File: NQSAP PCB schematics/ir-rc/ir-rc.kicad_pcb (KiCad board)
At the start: 2 copper layers, 102 x 96 mm, 6 parts, among them J1 Bus, J2 Bus, J3 Conn_02x08, J4 Conn_02x08, J5 Conn_02x08, J6 Conn_02x08

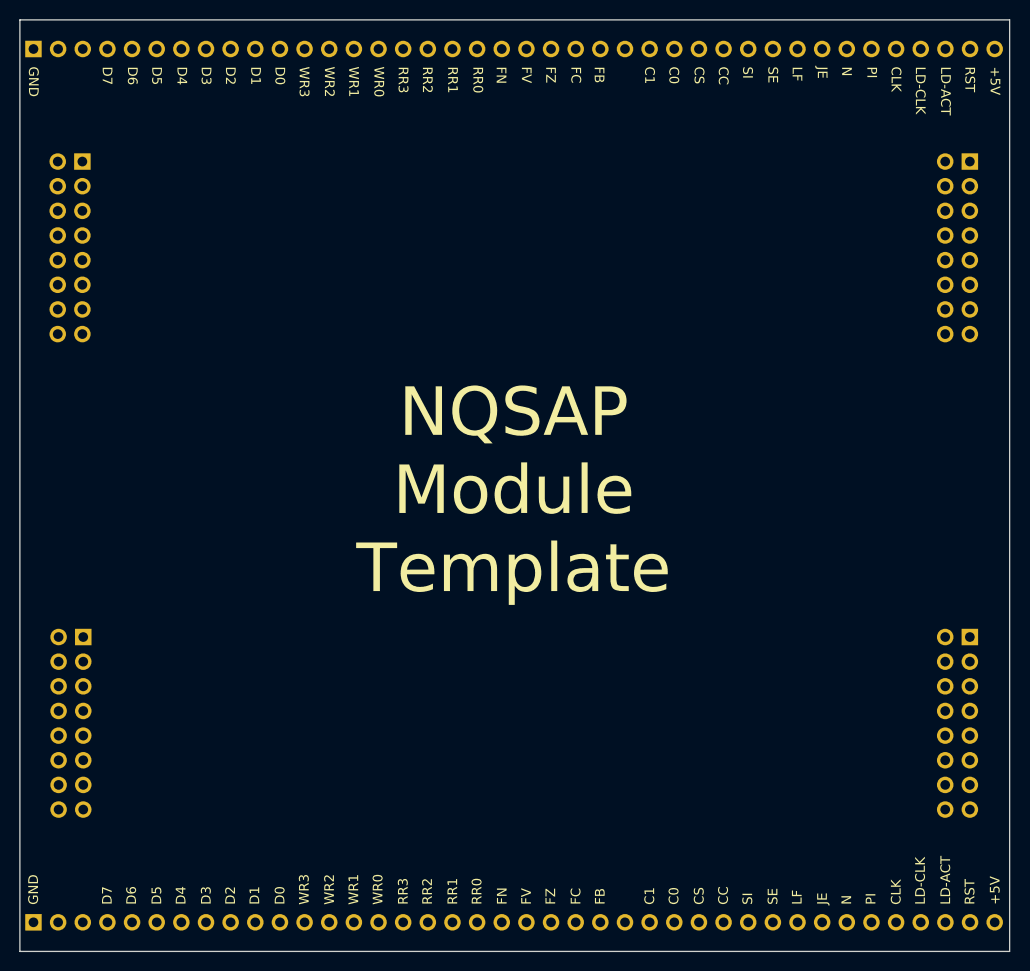
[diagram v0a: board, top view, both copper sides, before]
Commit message: Add Microcode and IR/RC modules.  Add clock circuit to Loader module.
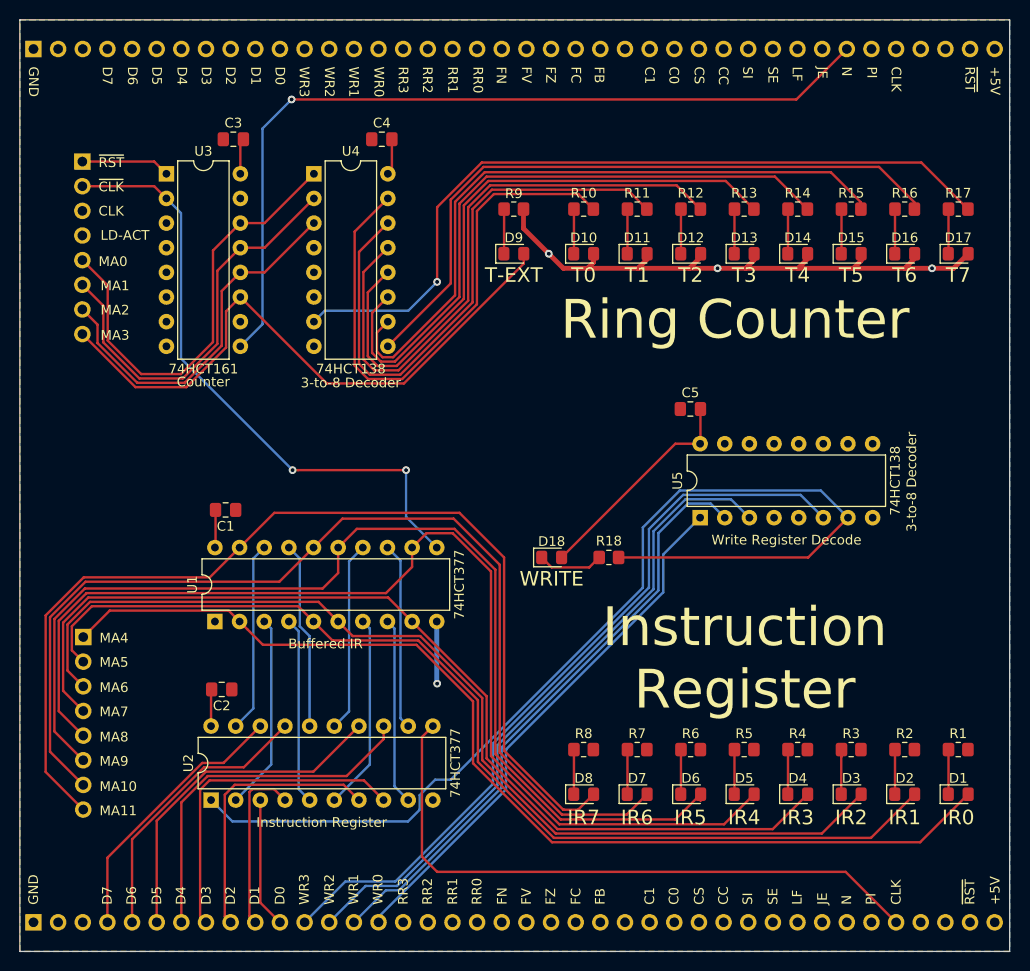
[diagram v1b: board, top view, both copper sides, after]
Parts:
- removed J5, J6: Conn_02x08, Connector_PinHeader_2.54mm:PinHeader_2x08_P2.54mm_Vertical
- added C1: 0.1uF, Capacitor_SMD:C_0805_2012Metric_Pad1.18x1.45mm_HandSolder, F.Cu at (106.2, 93.5)
- added C2: 0.1uF, Capacitor_SMD:C_0805_2012Metric_Pad1.18x1.45mm_HandSolder, F.Cu at (105.8, 112.0)
- added C3: 0.1uF, Capacitor_SMD:C_0805_2012Metric_Pad1.18x1.45mm_HandSolder, F.Cu at (107.0, 55.3)
- added C4: 0.1uF, Capacitor_SMD:C_0805_2012Metric_Pad1.18x1.45mm_HandSolder, F.Cu at (122.3, 55.3)
- added C5: 0.1uF, Capacitor_SMD:C_0805_2012Metric_Pad1.18x1.45mm_HandSolder, F.Cu at (154.1, 83.1)
- added D1: IR0, LED_SMD:LED_0805_2012Metric_Pad1.15x1.40mm_HandSolder, F.Cu at (181.7, 122.8)
- added D10: T0, LED_SMD:LED_0805_2012Metric_Pad1.15x1.40mm_HandSolder, F.Cu at (143.1, 67.1)
- added D11: T1, LED_SMD:LED_0805_2012Metric_Pad1.15x1.40mm_HandSolder, F.Cu at (148.6, 67.1)
- added D12: T2, LED_SMD:LED_0805_2012Metric_Pad1.15x1.40mm_HandSolder, F.Cu at (154.1, 67.1)
- added D13: T3, LED_SMD:LED_0805_2012Metric_Pad1.15x1.40mm_HandSolder, F.Cu at (159.6, 67.1)
- added D14: T4, LED_SMD:LED_0805_2012Metric_Pad1.15x1.40mm_HandSolder, F.Cu at (165.2, 67.1)
- added D15: T5, LED_SMD:LED_0805_2012Metric_Pad1.15x1.40mm_HandSolder, F.Cu at (170.7, 67.1)
- added D16: T6, LED_SMD:LED_0805_2012Metric_Pad1.15x1.40mm_HandSolder, F.Cu at (176.2, 67.1)
- added D17: T7, LED_SMD:LED_0805_2012Metric_Pad1.15x1.40mm_HandSolder, F.Cu at (181.7, 67.1)
- added D18: WRITE, LED_SMD:LED_0805_2012Metric_Pad1.15x1.40mm_HandSolder, F.Cu at (139.8, 98.4)
- added D2: IR1, LED_SMD:LED_0805_2012Metric_Pad1.15x1.40mm_HandSolder, F.Cu at (176.2, 122.8)
- added D3: IR2, LED_SMD:LED_0805_2012Metric_Pad1.15x1.40mm_HandSolder, F.Cu at (170.7, 122.8)
- added D4: IR3, LED_SMD:LED_0805_2012Metric_Pad1.15x1.40mm_HandSolder, F.Cu at (165.2, 122.8)
- added D5: IR4, LED_SMD:LED_0805_2012Metric_Pad1.15x1.40mm_HandSolder, F.Cu at (159.6, 122.8)
- added D6: IR5, LED_SMD:LED_0805_2012Metric_Pad1.15x1.40mm_HandSolder, F.Cu at (154.1, 122.8)
- added D7: IR6, LED_SMD:LED_0805_2012Metric_Pad1.15x1.40mm_HandSolder, F.Cu at (148.6, 122.8)
- added D8: IR7, LED_SMD:LED_0805_2012Metric_Pad1.15x1.40mm_HandSolder, F.Cu at (143.1, 122.8)
- added D9: T-EXT, LED_SMD:LED_0805_2012Metric_Pad1.15x1.40mm_HandSolder, F.Cu at (135.9, 67.1)
- added R1: R-GRN, Resistor_SMD:R_0805_2012Metric_Pad1.20x1.40mm_HandSolder, F.Cu at (181.7, 118.2)
- added R10: R-YEL, Resistor_SMD:R_0805_2012Metric_Pad1.20x1.40mm_HandSolder, F.Cu at (143.1, 62.5)
- added R11: R-YEL, Resistor_SMD:R_0805_2012Metric_Pad1.20x1.40mm_HandSolder, F.Cu at (148.6, 62.5)
- added R12: R-YEL, Resistor_SMD:R_0805_2012Metric_Pad1.20x1.40mm_HandSolder, F.Cu at (154.1, 62.5)
- added R13: R-YEL, Resistor_SMD:R_0805_2012Metric_Pad1.20x1.40mm_HandSolder, F.Cu at (159.6, 62.5)
- added R14: R-YEL, Resistor_SMD:R_0805_2012Metric_Pad1.20x1.40mm_HandSolder, F.Cu at (165.2, 62.5)
- added R15: R-YEL, Resistor_SMD:R_0805_2012Metric_Pad1.20x1.40mm_HandSolder, F.Cu at (170.7, 62.5)
- added R16: R-YEL, Resistor_SMD:R_0805_2012Metric_Pad1.20x1.40mm_HandSolder, F.Cu at (176.2, 62.5)
- added R17: R-YEL, Resistor_SMD:R_0805_2012Metric_Pad1.20x1.40mm_HandSolder, F.Cu at (181.7, 62.5)
- added R18: R-RED, Resistor_SMD:R_0805_2012Metric_Pad1.20x1.40mm_HandSolder, F.Cu at (145.7, 98.4)
- added R2: R-GRN, Resistor_SMD:R_0805_2012Metric_Pad1.20x1.40mm_HandSolder, F.Cu at (176.2, 118.2)
- added R3: R-GRN, Resistor_SMD:R_0805_2012Metric_Pad1.20x1.40mm_HandSolder, F.Cu at (170.7, 118.2)
- added R4: R-GRN, Resistor_SMD:R_0805_2012Metric_Pad1.20x1.40mm_HandSolder, F.Cu at (165.2, 118.2)
- added R5: R-GRN, Resistor_SMD:R_0805_2012Metric_Pad1.20x1.40mm_HandSolder, F.Cu at (159.6, 118.2)
- added R6: R-GRN, Resistor_SMD:R_0805_2012Metric_Pad1.20x1.40mm_HandSolder, F.Cu at (154.1, 118.2)
- added R7: R-GRN, Resistor_SMD:R_0805_2012Metric_Pad1.20x1.40mm_HandSolder, F.Cu at (148.6, 118.2)
- added R8: R-GRN, Resistor_SMD:R_0805_2012Metric_Pad1.20x1.40mm_HandSolder, F.Cu at (143.1, 118.2)
- added R9: R-WHT, Resistor_SMD:R_0805_2012Metric_Pad1.20x1.40mm_HandSolder, F.Cu at (135.9, 62.5)
- added U1: 74HCT377, Package_DIP:DIP-20_W7.62mm, F.Cu at (105.1, 105.0)
- added U2: 74HCT377, Package_DIP:DIP-20_W7.62mm, F.Cu at (104.7, 123.4)
- added U3: 74HCT161, Package_DIP:DIP-16_W7.62mm, F.Cu at (100.1, 58.9)
- added U4: 74HCT138, Package_DIP:DIP-16_W7.62mm, F.Cu at (115.3, 58.9)
- added U5: 74HCT138, Package_DIP:DIP-16_W7.62mm, F.Cu at (155.1, 94.3)
- J3, J4: footprint Connector_PinHeader_2.54mm:PinHeader_2x08_P2.54mm_Vertical -> Connector_PinHeader_2.54mm:PinHeader_1x08_P2.54mm_Vertical
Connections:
- net +5V renamed VCC
- J1 pad 10: D1 -> Net-(J1-Pad10)
- J1 pad 11: D0 -> Net-(J1-Pad11)
- J1 pad 12: WR3 -> Net-(J1-Pad12)
- J1 pad 13: WR2 -> Net-(J1-Pad13)
- J1 pad 14: WR1 -> Net-(J1-Pad14)
- J1 pad 15: WR0 -> Net-(J1-Pad15)
- J1 pad 16: RR3 -> Net-(J1-Pad16)
- J1 pad 17: RR2 -> Net-(J1-Pad17)
- J1 pad 18: RR1 -> Net-(J1-Pad18)
- J1 pad 19: RR0 -> Net-(J1-Pad19)
- J1 pad 2: NC-2 -> Net-(J1-Pad2)
- J1 pad 20: FN -> Net-(J1-Pad20)
- J1 pad 21: FV -> Net-(J1-Pad21)
- J1 pad 22: FZ -> Net-(J1-Pad22)
- J1 pad 23: FC -> Net-(J1-Pad23)
- J1 pad 24: FB -> Net-(J1-Pad24)
- J1 pad 25: XX0 -> Net-(J1-Pad25)
- J1 pad 26: C1 -> Net-(J1-Pad26)
- J1 pad 27: C0 -> Net-(J1-Pad27)
- J1 pad 28: CS -> Net-(J1-Pad28)
- J1 pad 29: CC -> Net-(J1-Pad29)
- J1 pad 3: NC-1 -> Net-(J1-Pad3)
- J1 pad 30: SI -> Net-(J1-Pad30)
- J1 pad 31: SE -> Net-(J1-Pad31)
- J1 pad 32: LF -> Net-(J1-Pad32)
- J1 pad 33: JE -> Net-(J1-Pad33)
- J1 pad 35: PI -> Net-(J1-Pad35)
- J1 pad 36: CLK -> Net-(J1-Pad36)
- J1 pad 37: LDR-CLK -> Net-(J1-Pad37)
- J1 pad 38: LDR-ACT -> Net-(J1-Pad38)
- J1 pad 39: RST -> Net-(J1-Pad39)
- J1 pad 4: D7 -> Net-(J1-Pad4)
- J1 pad 5: D6 -> Net-(J1-Pad5)
- J1 pad 6: D5 -> Net-(J1-Pad6)
- J1 pad 7: D4 -> Net-(J1-Pad7)
- J1 pad 8: D3 -> Net-(J1-Pad8)
- J1 pad 9: D2 -> Net-(J1-Pad9)
- J2 pad 16: RR3 -> Net-(J2-Pad16)
- J2 pad 17: RR2 -> Net-(J2-Pad17)
- J2 pad 18: RR1 -> Net-(J2-Pad18)
- J2 pad 19: RR0 -> Net-(J2-Pad19)
- J2 pad 2: NC-2 -> Net-(J2-Pad2)
- J2 pad 20: FN -> Net-(J2-Pad20)
- J2 pad 21: FV -> Net-(J2-Pad21)
- J2 pad 22: FZ -> Net-(J2-Pad22)
- J2 pad 23: FC -> Net-(J2-Pad23)
- J2 pad 24: FB -> Net-(J2-Pad24)
- J2 pad 25: XX0 -> Net-(J2-Pad25)
- J2 pad 26: C1 -> Net-(J2-Pad26)
- J2 pad 27: C0 -> Net-(J2-Pad27)
- J2 pad 28: CS -> Net-(J2-Pad28)
- J2 pad 29: CC -> Net-(J2-Pad29)
- J2 pad 3: NC-1 -> Net-(J2-Pad3)
- J2 pad 30: SI -> Net-(J2-Pad30)
- J2 pad 31: SE -> Net-(J2-Pad31)
- J2 pad 32: LF -> Net-(J2-Pad32)
- J2 pad 33: JE -> Net-(J2-Pad33)
- J2 pad 34: N -> Net-(J2-Pad34)
- J2 pad 35: PI -> Net-(J2-Pad35)
- J2 pad 37: LDR-CLK -> Net-(J2-Pad37)
- J2 pad 38: LDR-ACT -> Net-(J2-Pad38)
- J2 pad 39: RST -> Net-(J2-Pad39)
- J3 pad 1: Net-(J3-Pad1) -> ~RST
- J3 pad 2: Net-(J3-Pad2) -> ~CLK
- J3 pad 5: Net-(J3-Pad5) -> MA0
- J3 pad 6: Net-(J3-Pad6) -> MA1
- J3 pad 7: Net-(J3-Pad7) -> MA2
- J3 pad 8: Net-(J3-Pad8) -> MA3
- J4 pad 1: Net-(J4-Pad1) -> MA4
- J4 pad 2: Net-(J4-Pad2) -> MA5
- J4 pad 3: Net-(J4-Pad3) -> MA6
- J4 pad 4: Net-(J4-Pad4) -> MA7
- J4 pad 5: Net-(J4-Pad5) -> MA8
- J4 pad 6: Net-(J4-Pad6) -> MA9
- J4 pad 7: Net-(J4-Pad7) -> MA10
- J4 pad 8: Net-(J4-Pad8) -> MA11
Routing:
- net MA8: track 0.00 -> 114.3 mm
- net MA9: track 0.00 -> 113.1 mm
- net ~WI: track 0.00 -> 111.7 mm
- net MA10: track 0.00 -> 109.3 mm
- net MA4: track 0.00 -> 108.0 mm
- net MA11: track 0.00 -> 107.6 mm
- net MA5: track 0.00 -> 107.3 mm
- net MA6: track 0.00 -> 105.1 mm
- net MA7: track 0.00 -> 102.9 mm
- net VCC: track 0.00 -> 101.2 mm, vias 0 -> 3
- net N: track 0.00 -> 87.0 mm, vias 0 -> 1
- net Net-(R17-Pad2): track 0.00 -> 80.7 mm, vias 0 -> 1
- net WR3: track 0.00 -> 78.6 mm
- net Net-(R16-Pad2): track 0.00 -> 69.2 mm
- net Net-(R15-Pad2): track 0.00 -> 69.2 mm
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- added copper zone on F.Cu, net GND
- added copper zone on B.Cu, net VCC
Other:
- board text added: "Instruction Register"
- board text added: "MA0"
- board text added: "MA1"
- board text added: "MA10"
- board text added: "MA11"
- board text added: "MA2"
- board text added: "MA3"
- board text added: "MA4"
- board text added: "MA5"
- board text added: "MA6"
- board text added: "MA7"
- board text added: "MA8"
- board text added: "MA9"
- board text added: "Ring Counter"
- board text added: "~CLK"
- board text added: "~RST"
- board text removed: "LD-CLK"
- board text removed: "NQSAP Module Template"
- board text removed: "RST"

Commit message: Add RAM, update and add gerbers for new boards
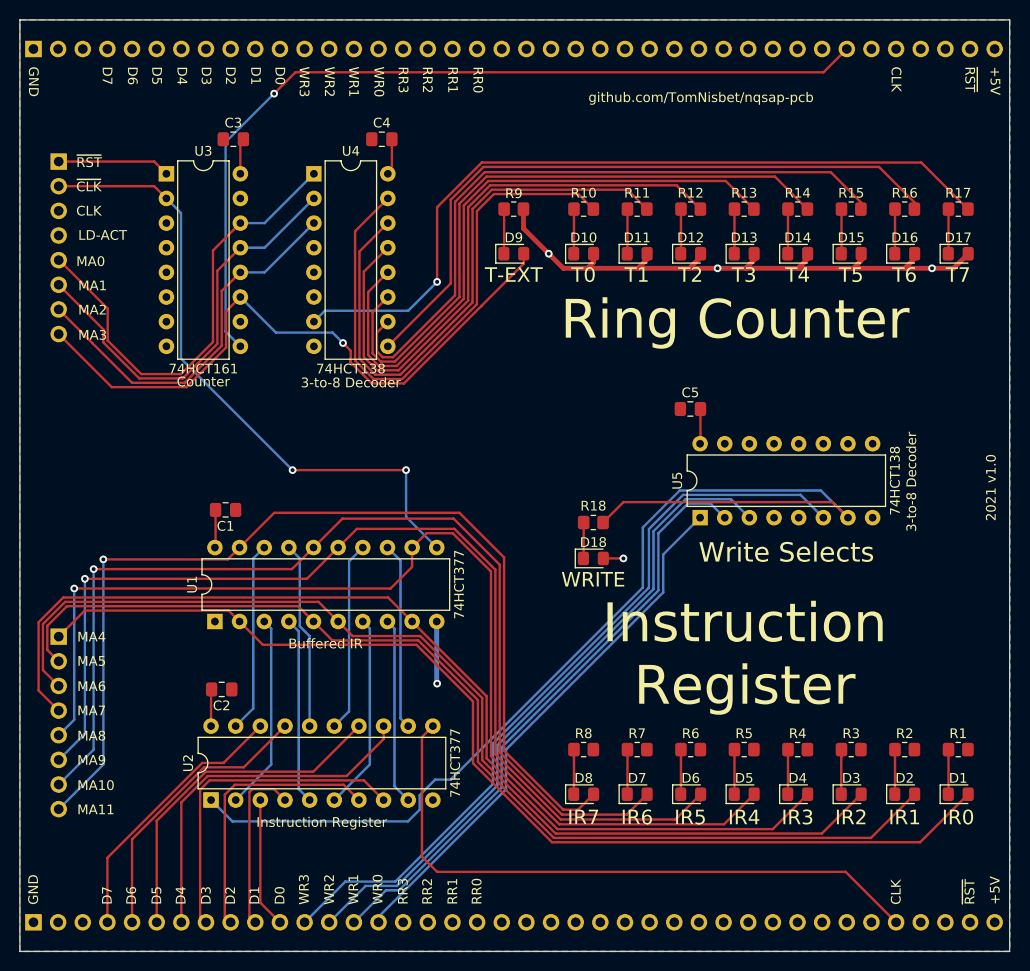
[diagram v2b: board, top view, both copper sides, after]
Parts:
- moved D18 4.30 mm to (144.1, 98.5)
- moved R18 3.94 mm to (144.1, 94.8)
- moved J4 2.53 mm to (89.0, 106.6)
- moved J3 2.44 mm to (89.0, 57.6)
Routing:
- net VCC: track 101.2 -> 84.1 mm, vias 3 -> 4
- net MA3: track 63.9 -> 67.5 mm, vias 0 -> 1
- net Net-(D18-Pad1): track 6.77 -> 3.71 mm
- net N: track 87.0 -> 89.7 mm
- net MA7: track 102.9 -> 105.4 mm
- net MA6: track 105.1 -> 107.6 mm
- net MA4: track 108.0 -> 110.5 mm
- net MA5: track 107.3 -> 109.8 mm
- net ~RST: track 9.18 -> 11.6 mm
- net ~CLK: track 63.6 -> 66.0 mm
- net MA9: track 113.1 -> 110.7 mm, vias 0 -> 1
- net MA11: track 107.6 -> 105.3 mm, vias 0 -> 1
- net MA10: track 109.3 -> 107.7 mm, vias 0 -> 1
- net ~WI: track 111.7 -> 113.1 mm
- net MA2: track 38.2 -> 39.5 mm
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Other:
- board text added: "2021 v1.0"
- board text added: "github.com/TomNisbet/nqsap-pcb"
- board text removed: "C0"
- board text removed: "C1"
- board text removed: "CC"
- board text removed: "CS"
- board text removed: "FB"
- board text removed: "FC"
- board text removed: "FN"
- board text removed: "FV"
- board text removed: "FZ"
- board text removed: "JE"
- board text removed: "LF"
- board text removed: "N"
- board text removed: "PI"
- board text removed: "SE"
- board text removed: "SI"

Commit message: updated KiCads and gerbers for the AB Registers and IR/RC module
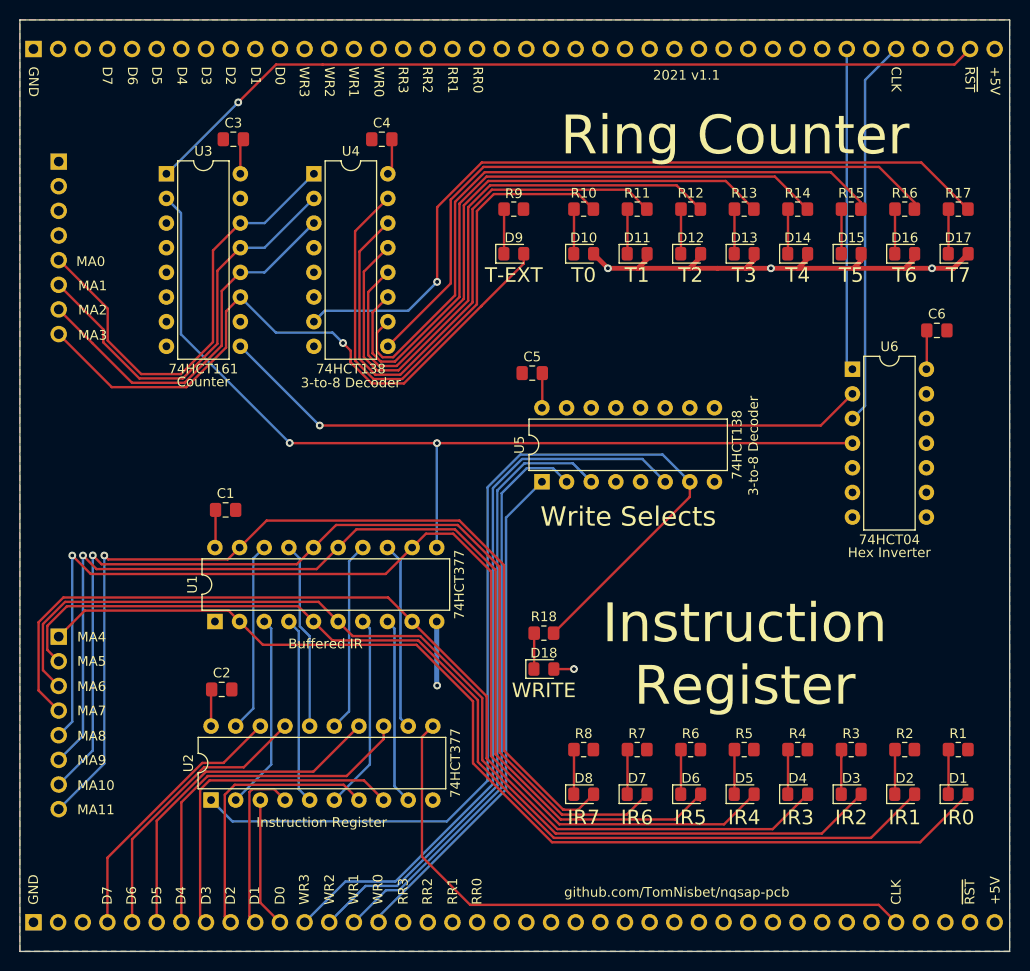
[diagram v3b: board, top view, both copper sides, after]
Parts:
- added C6: 0.1uF, Capacitor_SMD:C_0805_2012Metric_Pad1.18x1.45mm_HandSolder, F.Cu at (179.5, 75.0)
- added U6: 74HCT04, Package_DIP:DIP-14_W7.62mm, F.Cu at (170.8, 79.0)
- moved U5 16.7 mm to (138.8, 90.6)
- moved C5 16.7 mm to (137.8, 79.4)
- moved D18 12.5 mm to (139.0, 109.9)
- moved R18 12.5 mm to (139.0, 106.2)
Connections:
- J1 pad 36: Net-(J1-Pad36) -> CLK
- J1 pad 39: Net-(J1-Pad39) -> ~RST
- J3 pad 1: ~RST -> Net-(J3-Pad1)
- J3 pad 2: ~CLK -> Net-(J3-Pad2)
- R9 pad 1: VCC -> GND
- U3 pad 9: N -> Net-(U3-Pad9)
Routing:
- net ~RST: track 11.6 -> 88.1 mm, vias 0 -> 1
- net Net-(U3-Pad9): track 0.00 -> 67.8 mm, vias 0 -> 1
- net N: track 89.7 -> 33.2 mm, vias 1 -> 0
- net CLK: track 65.6 -> 105.5 mm
- net ~CLK: track 66.0 -> 99.2 mm
- net VCC: track 84.1 -> 76.1 mm
- net ~WI: track 113.1 -> 106.2 mm
- net WR0: track 55.4 -> 52.4 mm
- net WR1: track 62.6 -> 59.7 mm
- net WR3: track 78.6 -> 75.8 mm
- net WR2: track 68.1 -> 65.2 mm
- net MA9: track 110.7 -> 113.3 mm
- net MA8: track 114.2 -> 116.7 mm
- net MA10: track 107.7 -> 108.7 mm
- net MA11: track 105.3 -> 104.7 mm
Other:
- board text added: "2021 v1.1"
- board text removed: "2021 v1.0"
- board text removed: "LD-ACT"
- board text removed: "~CLK"
